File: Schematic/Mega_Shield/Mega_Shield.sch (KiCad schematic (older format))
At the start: 25 parts, among them J1 Mini-DIN-4, J10 Conn_01x08, J11 Conn_01x08, J12 Conn_02x18_Odd_Even, J13 Conn_01x08, J14 Conn_01x08, J15 Conn_01x08, J16 Conn_01x10, J2 Mini-DIN-4, J3 Mini-DIN-4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

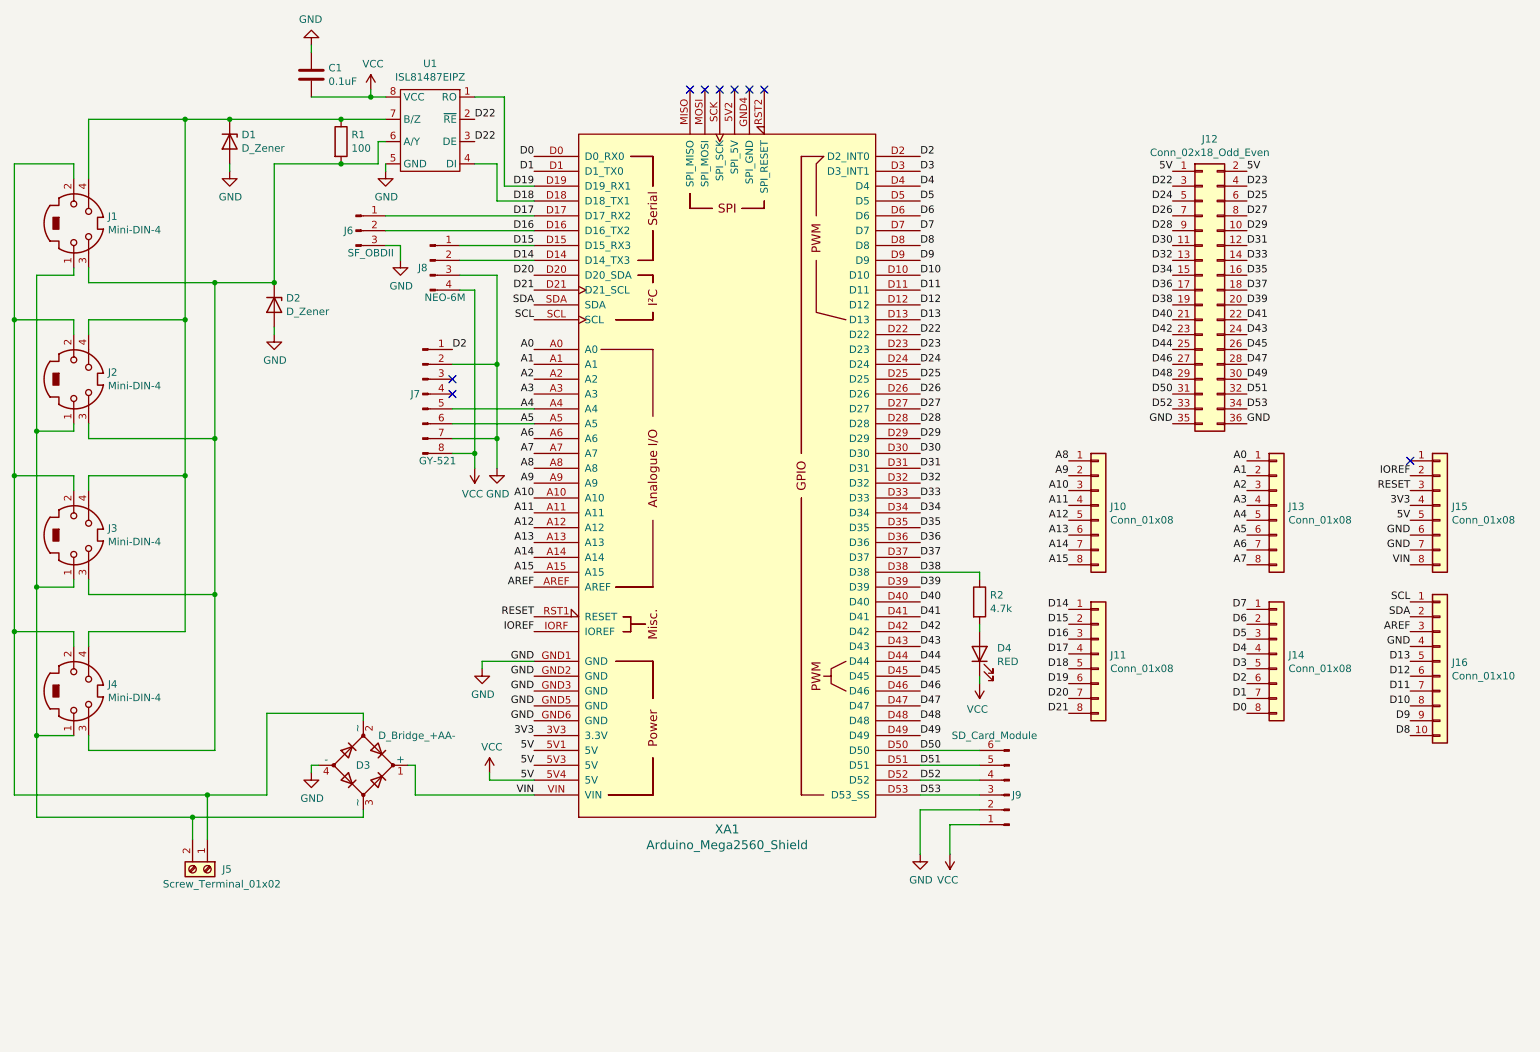
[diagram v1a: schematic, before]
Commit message: Fixed schematic issues. Made code for TTS transmit
Schematic issues documented on Trello card fixed. TTS differential wire transmit code for the TTS implemented. Still need to do auto adressing and time stamp transmission.

2.2 Basic Sensor Suite
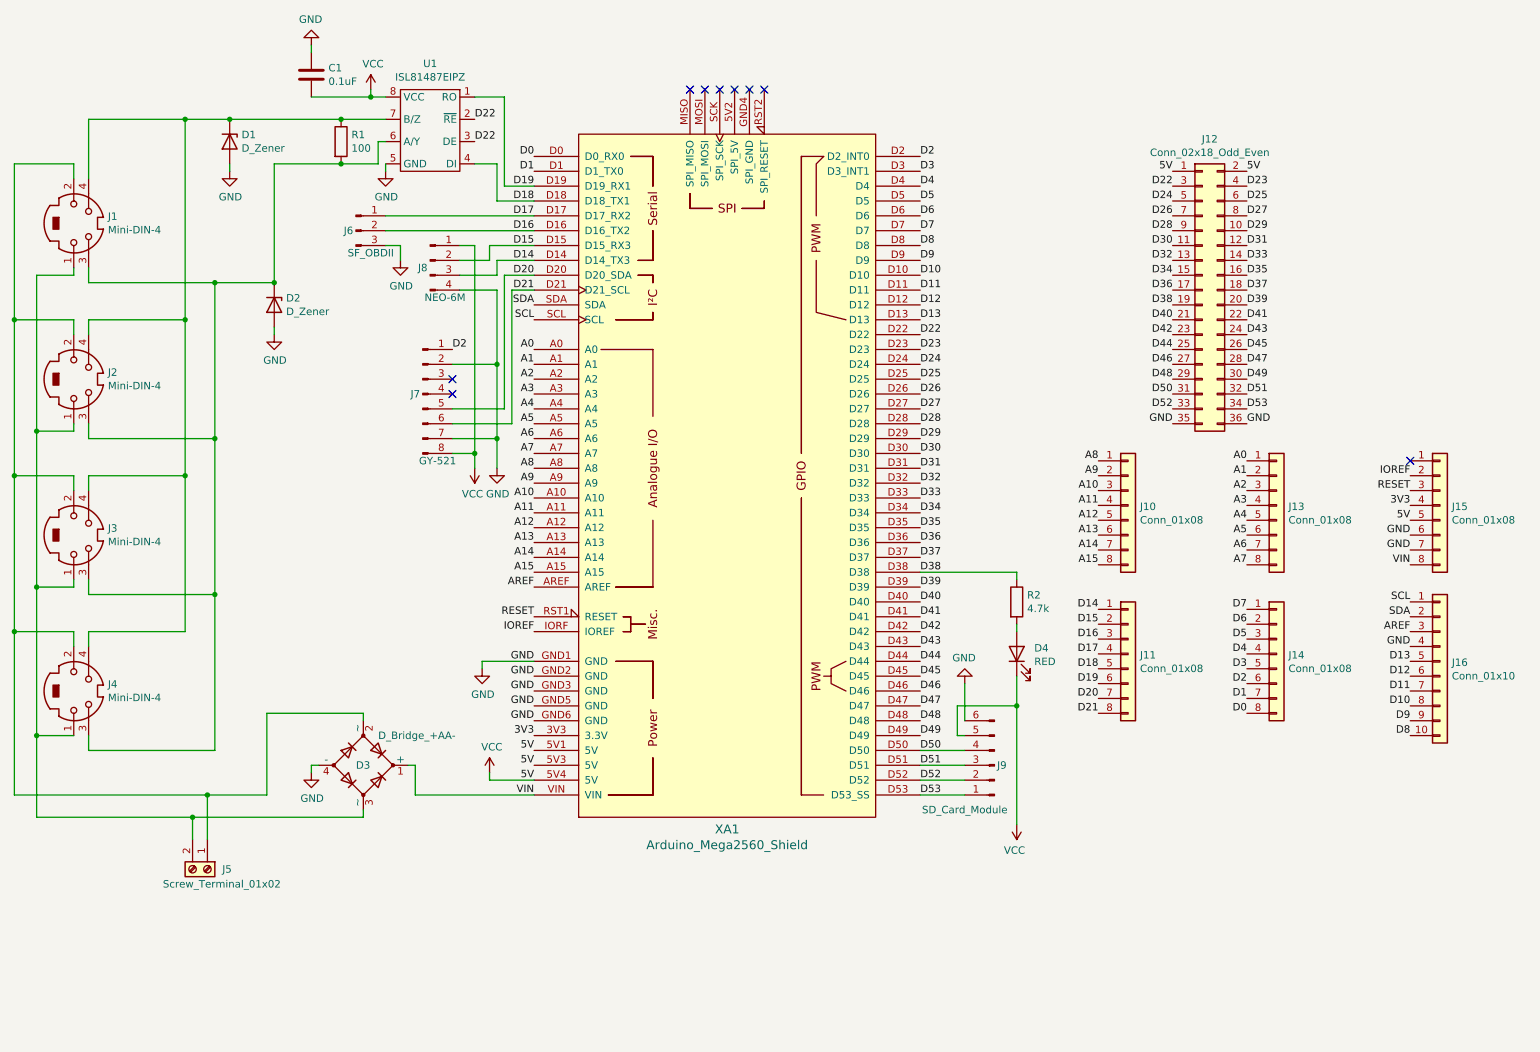
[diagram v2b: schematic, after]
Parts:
- J12: footprint Connector_PinSocket_2.54mm:PinSocket_2x18_P2.54mm_Vertical -> TTS-UART:PinSocket_2x18_P2.54mm_Vertical_Swapped
- R1: footprint Resistor_THT:R_Axial_DIN0309_L9.0mm_D3.2mm_P12.70mm_Horizontal -> Resistor_THT:R_Axial_DIN0207_L6.3mm_D2.5mm_P7.62mm_Horizontal
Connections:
- net A4: no longer J7.5 (Pin_5)
- net A5: no longer J7.6 (Pin_6)
- net D14: now also J8.3 (Pin_3); no longer J8.2 (Pin_2)
- net D15: now also J8.2 (Pin_2); no longer J8.1 (Pin_1)
- net D20: now also J7.5 (Pin_5)
- net D21: now also J7.6 (Pin_6)
- net D50: now also J9.4 (Pin_4); no longer J9.6 (Pin_6)
- net D51: now also J9.3 (Pin_3); no longer J9.5 (Pin_5)
- net D52: now also J9.2 (Pin_2); no longer J9.4 (Pin_4)
- net D53: now also J9.1 (Pin_1); no longer J9.3 (Pin_3)
- net GND: now also J8.4 (Pin_4), J9.6 (Pin_6); no longer J8.3 (Pin_3), J9.2 (Pin_2)
- net VCC: now also J8.1 (Pin_1), J9.5 (Pin_5); no longer J8.4 (Pin_4), J9.1 (Pin_1)
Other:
- moved on the sheet: D4, J10, J11, J9, R2
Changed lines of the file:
@@
 $EndDescr
-$Comp
-L arduino:Arduino_Mega2560_Shield XA1
-U 1 1 5F8E6D38
-P 5650 3700
-F 0 "XA1" H 5650 1319 60  0000 C CNN
-F 1 "Arduino_Mega2560_Shield" H 5650 1213 60  0000 C CNN
-F 2 "Arduino:Arduino_Mega2560_Shield" H 6350 6450 60  0001 C CNN
-F 3 "https://store.arduino.cc/arduino-mega-2560-rev3" H 6350 6450 60  0001 C CNN
-	1    5650 3700
-	1    0    0    -1
-$EndComp
 $Comp
 L Connector:Conn_01x06_Male J9
 U 1 1 5F8F3F29
-P 7550 5850
-F 0 "J9" H 7500 5850 50  0000 C CNN
-F 1 "SD_Card_Module" H 7650 5450 50  0000 C CNN
-F 2 "Onboard_Sensors:SD_Module" H 7550 5850 50  0001 C CNN
-F 3 "~" H 7550 5850 50  0001 C CNN
-	1    7550 5850
+P 7450 5650
+F 0 "J9" H 7400 5650 50  0000 C CNN
+F 1 "SD_Card_Module" H 7650 5950 50  0000 C CNN
+F 2 "Onboard_Sensors:SD_Module" H 7450 5650 50  0001 C CNN
+F 3 "~" H 7450 5650 50  0001 C CNN
+	1    7450 5650
 	-1   0    0    1
 $EndComp
@@
 F 0 "R1" H 3120 1496 50  0000 L CNN
 F 1 "100" H 3120 1405 50  0000 L CNN
-F 2 "Resistor_THT:R_Axial_DIN0309_L9.0mm_D3.2mm_P12.70mm_Horizontal" V 2980 1450 50  0001 C CNN
+F 2 "Resistor_THT:R_Axial_DIN0207_L6.3mm_D2.5mm_P7.62mm_Horizontal" V 2980 1450 50  0001 C CNN
 F 3 "~" H 3050 1450 50  0001 C CNN
 	1    3050 1450
@@
 L power:VCC #PWR017
 U 1 1 5F90DE60
-P 7150 6250
-F 0 "#PWR017" H 7150 6100 50  0001 C CNN
-F 1 "VCC" H 7165 6423 50  0000 C CNN
-F 2 "" H 7150 6250 50  0001 C CNN
-F 3 "" H 7150 6250 50  0001 C CNN
-	1    7150 6250
+P 7600 6050
+F 0 "#PWR017" H 7600 5900 50  0001 C CNN
+F 1 "VCC" H 7615 6223 50  0000 C CNN
+F 2 "" H 7600 6050 50  0001 C CNN
+F 3 "" H 7600 6050 50  0001 C CNN
+	1    7600 6050
 	-1   0    0    1
 $EndComp
@@
 L power:GND #PWR016
 U 1 1 5F9126E2
-P 6950 6250
-F 0 "#PWR016" H 6950 6000 50  0001 C CNN
-F 1 "GND" H 6955 6077 50  0000 C CNN
-F 2 "" H 6950 6250 50  0001 C CNN
-F 3 "" H 6950 6250 50  0001 C CNN
-	1    6950 6250
-	1    0    0    -1
-$EndComp
-Wire Wire Line
-	7150 6250 7150 6050
-Wire Wire Line
-	7150 6050 7350 6050
-Wire Wire Line
-	6950 6250 6950 5950
-Wire Wire Line
-	6950 5950 7350 5950
-Wire Wire Line
-	7350 5550 6950 5550
-Wire Wire Line
-	6950 5650 7350 5650
-Wire Wire Line
-	7350 5750 6950 5750
-Wire Wire Line
-	6950 5850 7350 5850
-Wire Wire Line
-	3800 3250 4350 3250
-Wire Wire Line
-	4350 3350 3800 3350
+P 7250 5100
+F 0 "#PWR016" H 7250 4850 50  0001 C CNN
+F 1 "GND" H 7255 4927 50  0000 C CNN
+F 2 "" H 7250 5100 50  0001 C CNN
+F 3 "" H 7250 5100 50  0001 C CNN
+	1    7250 5100
+	-1   0    0    1
+$EndComp
 Text Label 6950 1550 0    50   ~ 0
 D2
@@
 $EndComp
 Wire Wire Line
-	3850 2150 4350 2150
-Wire Wire Line
-	3850 2250 4350 2250
-Wire Wire Line
 	4100 3450 4100 3650
 Connection ~ 4100 3450
 Wire Wire Line
 	3800 3450 4100 3450
-Wire Wire Line
-	3850 2350 4100 2350
-Wire Wire Line
-	3950 2450 3850 2450
-Wire Wire Line
-	3950 2450 3950 3550
-Connection ~ 3950 3550
 $Comp
 L power:GND #PWR011
@@
 F 0 "J12" H 8900 3467 50  0000 C CNN
 F 1 "Conn_02x18_Odd_Even" H 8900 3376 50  0000 C CNN
-F 2 "Connector_PinSocket_2.54mm:PinSocket_2x18_P2.54mm_Vertical" H 8850 2450 50  0001 C CNN
+F 2 "TTS-UART:PinSocket_2x18_P2.54mm_Vertical_Swapped" H 8850 2450 50  0001 C CNN
 F 3 "~" H 8850 2450 50  0001 C CNN
 	1    8850 2450
@@
 Text Label 10250 4300 2    50   ~ 0
 VIN
-Text Label 7950 4600 2    50   ~ 0
+Text Label 8150 4600 2    50   ~ 0
 D14
-Text Label 7950 4700 2    50   ~ 0
+Text Label 8150 4700 2    50   ~ 0
 D15
-Text Label 7950 4800 2    50   ~ 0
+Text Label 8150 4800 2    50   ~ 0
 D16
-Text Label 7950 4900 2    50   ~ 0
+Text Label 8150 4900 2    50   ~ 0
 D17
-Text Label 7950 5000 2    50   ~ 0
+Text Label 8150 5000 2    50   ~ 0
 D18
-Text Label 7950 5100 2    50   ~ 0
+Text Label 8150 5100 2    50   ~ 0
 D19
-Text Label 7950 5200 2    50   ~ 0
+Text Label 8150 5200 2    50   ~ 0
 D20
-Text Label 7950 5300 2    50   ~ 0
+Text Label 8150 5300 2    50   ~ 0
 D21
 $Comp
 L Connector_Generic:Conn_01x08 J11
 U 1 1 5FA0B0B6
-P 8150 4900
-F 0 "J11" H 8230 4892 50  0000 L CNN
-F 1 "Conn_01x08" H 8230 4801 50  0000 L CNN
-F 2 "Connector_PinSocket_2.54mm:PinSocket_1x08_P2.54mm_Vertical" H 8150 4900 50  0001 C CNN
-F 3 "~" H 8150 4900 50  0001 C CNN
-	1    8150 4900
+P 8350 4900
+F 0 "J11" H 8430 4892 50  0000 L CNN
+F 1 "Conn_01x08" H 8430 4801 50  0000 L CNN
+F 2 "Connector_PinSocket_2.54mm:PinSocket_1x08_P2.54mm_Vertical" H 8350 4900 50  0001 C CNN
+F 3 "~" H 8350 4900 50  0001 C CNN
+	1    8350 4900
 	1    0    0    -1
 $EndComp
@@
 L Connector_Generic:Conn_01x08 J10
 U 1 1 5F9F881C
-P 8150 3900
-F 0 "J10" H 8230 3892 50  0000 L CNN
-F 1 "Conn_01x08" H 8230 3801 50  0000 L CNN
-F 2 "Connector_PinSocket_2.54mm:PinSocket_1x08_P2.54mm_Vertical" H 8150 3900 50  0001 C CNN
-F 3 "~" H 8150 3900 50  0001 C CNN
-	1    8150 3900
+P 8350 3900
+F 0 "J10" H 8430 3892 50  0000 L CNN
+F 1 "Conn_01x08" H 8430 3801 50  0000 L CNN
+F 2 "Connector_PinSocket_2.54mm:PinSocket_1x08_P2.54mm_Vertical" H 8350 3900 50  0001 C CNN
+F 3 "~" H 8350 3900 50  0001 C CNN
+	1    8350 3900
 	1    0    0    -1
 $EndComp
 Text Label 10250 5450 2    50   ~ 0
 D8
-Text Label 7950 3600 2    50   ~ 0
+Text Label 8150 3600 2    50   ~ 0
 A8
-Text Label 7950 3700 2    50   ~ 0
+Text Label 8150 3700 2    50   ~ 0
 A9
-Text Label 7950 3800 2    50   ~ 0
+Text Label 8150 3800 2    50   ~ 0
 A10
-Text Label 7950 3900 2    50   ~ 0
+Text Label 8150 3900 2    50   ~ 0
 A11
-Text Label 7950 4000 2    50   ~ 0
+Text Label 8150 4000 2    50   ~ 0
 A12
-Text Label 7950 4100 2    50   ~ 0
+Text Label 8150 4100 2    50   ~ 0
 A13
-Text Label 7950 4200 2    50   ~ 0
+Text Label 8150 4200 2    50   ~ 0
 A14
-Text Label 7950 4300 2    50   ~ 0
+Text Label 8150 4300 2    50   ~ 0
 A15
 Text Label 9150 3600 2    50   ~ 0
@@
 $EndComp
 Wire Wire Line
-	4100 2350 4100 2950
-Wire Wire Line
 	3800 2950 4100 2950
-Connection ~ 4100 2950
 Wire Wire Line
 	4100 2950 4100 3450
@@
 L Device:LED D4
 U 1 1 5F920F36
-P 7350 4900
-F 0 "D4" V 7389 4782 50  0000 R CNN
-F 1 "RED" V 7298 4782 50  0000 R CNN
-F 2 "digikey-kicad-library:LED_3mm_Radial" H 7350 4900 50  0001 C CNN
-F 3 "~" H 7350 4900 50  0001 C CNN
-	1    7350 4900
+P 7600 4900
+F 0 "D4" V 7639 4782 50  0000 R CNN
+F 1 "RED" V 7548 4782 50  0000 R CNN
+F 2 "digikey-kicad-library:LED_3mm_Radial" H 7600 4900 50  0001 C CNN
+F 3 "~" H 7600 4900 50  0001 C CNN
+	1    7600 4900
 	0    -1   -1   0
 $EndComp
 Wire Wire Line
-	6950 4350 7350 4350
-Wire Wire Line
-	7350 4350 7350 4400
-Wire Wire Line
-	7350 5100 7350 5050
+	7600 4350 7600 4400
 $Comp
 L Device:D_Bridge_+AA- D3
@@
 	3550 5850 4350 5850
 $Comp
-L power:VCC #PWR02
-U 1 1 5FA4D1B3
-P 7350 5100
-F 0 "#PWR02" H 7350 4950 50  0001 C CNN
-F 1 "VCC" H 7365 5273 50  0000 C CNN
-F 2 "" H 7350 5100 50  0001 C CNN
-F 3 "" H 7350 5100 50  0001 C CNN
-	1    7350 5100
-	-1   0    0    1
-$EndComp
-$Comp
 L Device:R R2
 U 1 1 5FA529EF
-P 7350 4550
-F 0 "R2" H 7420 4596 50  0000 L CNN
-F 1 "4.7k" H 7420 4505 50  0000 L CNN
-F 2 "Resistor_THT:R_Axial_DIN0204_L3.6mm_D1.6mm_P5.08mm_Horizontal" V 7280 4550 50  0001 C CNN
-F 3 "~" H 7350 4550 50  0001 C CNN
-	1    7350 4550
-	1    0    0    -1
-$EndComp
-Wire Wire Line
-	7350 4700 7350 4750
+P 7600 4550
+F 0 "R2" H 7670 4596 50  0000 L CNN
+F 1 "4.7k" H 7670 4505 50  0000 L CNN
+F 2 "Resistor_THT:R_Axial_DIN0204_L3.6mm_D1.6mm_P5.08mm_Horizontal" V 7530 4550 50  0001 C CNN
+F 3 "~" H 7600 4550 50  0001 C CNN
+	1    7600 4550
+	1    0    0    -1
+$EndComp
+Wire Wire Line
+	7600 4700 7600 4750
+Wire Wire Line
+	6950 4350 7600 4350
+$Comp
+L arduino:Arduino_Mega2560_Shield XA1
+U 1 1 5F8E6D38
+P 5650 3700
+F 0 "XA1" H 5650 1319 60  0000 C CNN
+F 1 "Arduino_Mega2560_Shield" H 5650 1213 60  0000 C CNN
+F 2 "Arduino:Arduino_Mega2560_Shield" H 6350 6450 60  0001 C CNN
+F 3 "https://store.arduino.cc/arduino-mega-2560-rev3" H 6350 6450 60  0001 C CNN
+	1    5650 3700
+	1    0    0    -1
+$EndComp
+Wire Wire Line
+	6950 5650 7250 5650
+Wire Wire Line
+	7250 5550 6950 5550
+Wire Wire Line
+	7250 5750 6950 5750
+Wire Wire Line
+	7250 5850 6950 5850
+Wire Wire Line
+	7250 5350 7250 5100
+Wire Wire Line
+	7250 5450 7200 5450
+Wire Wire Line
+	7200 5450 7200 5250
+Wire Wire Line
+	7200 5250 7600 5250
+Wire Wire Line
+	7600 5050 7600 5250
+Wire Wire Line
+	7600 5250 7600 6050
+Connection ~ 7600 5250
+Wire Wire Line
+	4150 3250 3800 3250
+Wire Wire Line
+	3800 3350 4200 3350
+Wire Wire Line
+	4350 2350 4150 2350
+Wire Wire Line
+	4350 2450 4200 2450
+Wire Wire Line
+	4150 2350 4150 3250
+Wire Wire Line
+	4200 2450 4200 3350
+Wire Wire Line
+	3850 2150 3950 2150
+Wire Wire Line
+	3950 2150 3950 3550
+Connection ~ 3950 3550
+Wire Wire Line
+	3850 2450 4100 2450
+Wire Wire Line
+	4100 2450 4100 2950
+Connection ~ 4100 2950
+Wire Wire Line
+	3850 2350 4100 2350
+Wire Wire Line
+	4100 2250 4350 2250
+Wire Wire Line
+	4100 2350 4100 2250
+Wire Wire Line
+	3850 2250 4050 2250
+Wire Wire Line
+	4050 2150 4350 2150
+Wire Wire Line
+	4050 2250 4050 2150
 $EndSCHEMATC

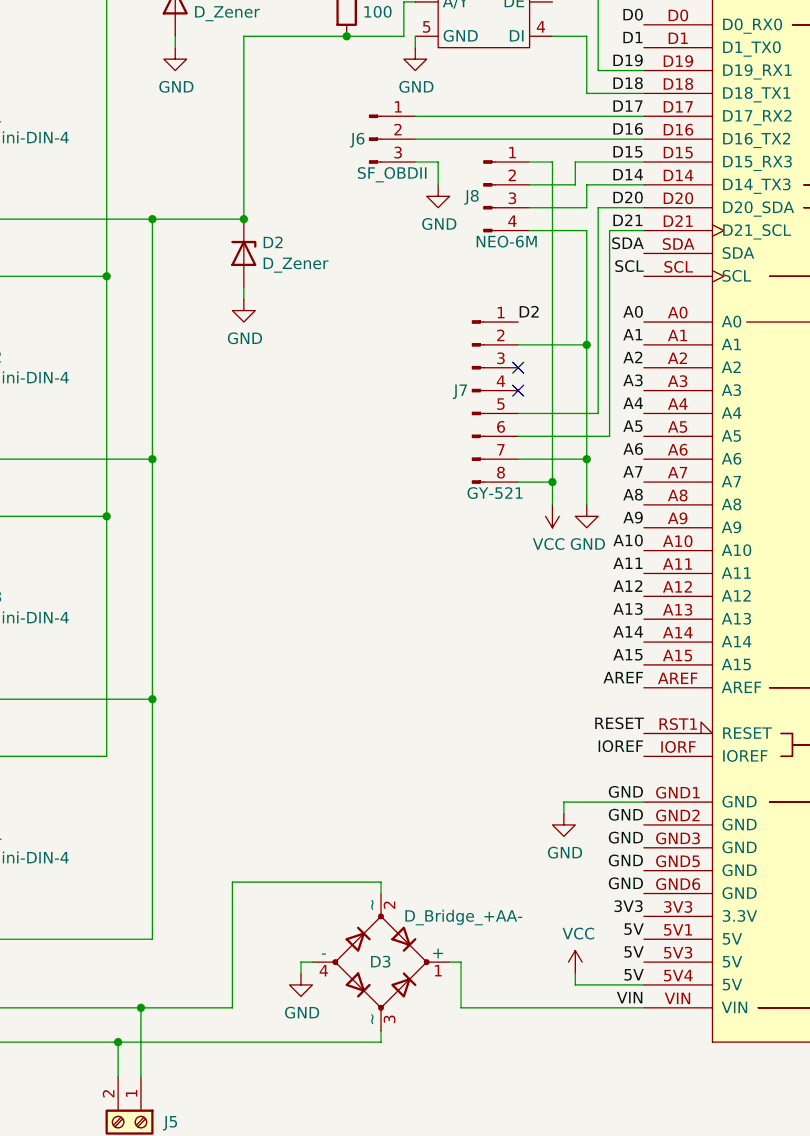
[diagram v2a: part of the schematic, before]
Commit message: Integration of IMU + comms algo upgrade.
Upgraded comms method to use switch/case method. Integrade the IMU board onto the Mega shield.

2.2 Basic Sensor Suite
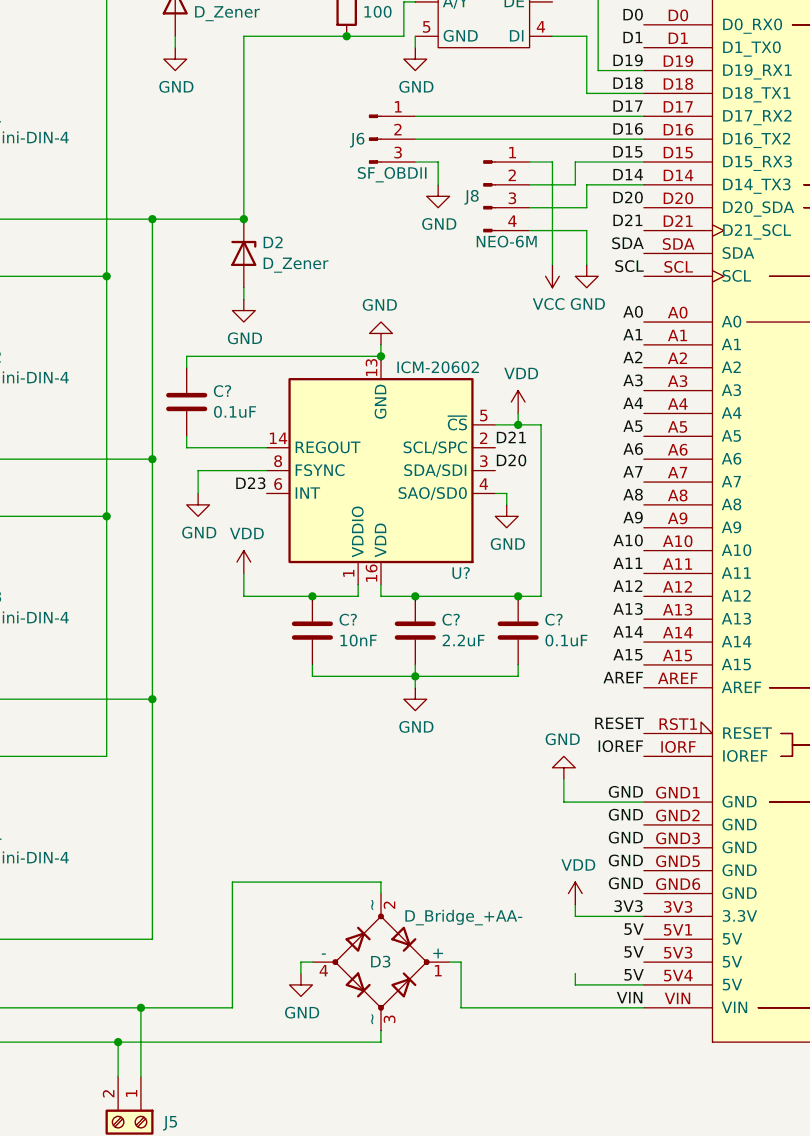
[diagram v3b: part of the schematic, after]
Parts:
- removed J7: GY-521, Onboard_Sensors:GY-521, symbol Connector:Conn_01x08_Male
- added C?: 2.2uF, Capacitor_THT:C_Rect_L4.0mm_W2.5mm_P2.50mm, symbol Device:C
- added C? (x2): 0.1uF, Capacitor_THT:C_Rect_L4.0mm_W2.5mm_P2.50mm, symbol Device:C
- added C?: 10nF, Capacitor_THT:C_Rect_L4.0mm_W2.5mm_P2.50mm, symbol Device:C
- added U?: ICM-20602, Package_LGA:LGA-16_3x3mm_P0.5mm_LayoutBorder3x5y, symbol Sensor_Motion:ICM-20602
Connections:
- net D20: now also U?.3 (SDA/SDI)
- net D21: now also U?.2 (SCL/SPC)
- net D23: now also U?.6 (INT)
- net GND: now also C?.1, C?.2, C?.2, C?.2, U?.10 (GND), U?.11 (GND), U?.12 (GND), U?.13 (GND), U?.15 (GND), U?.4 (SAO/SD0), U?.8 (FSYNC), U?.9 (GND)
- net VCC: no longer J12.1 (Pin_1), J12.2 (Pin_2), J15.5 (Pin_5), XA1.5V1 (5V), XA1.5V3 (5V), XA1.5V4 (5V)
- net 3V3 renamed VDD
- net VDD: now also C?.1, C?.1, C?.1, U?.1 (VDDIO), U?.16 (VDD), U?.5 (~CS)
- new net: C?.2, U?.14 (REGOUT)
- new net 5V: J12.1 (Pin_1), J12.2 (Pin_2), J15.5 (Pin_5), XA1.5V1 (5V), XA1.5V3 (5V), XA1.5V4 (5V)
- no-connect marks 9 -> 7
